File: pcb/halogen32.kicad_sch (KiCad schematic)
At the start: 13 parts, among them SW1 SW_SPDT, U1 STM32F411CEUx

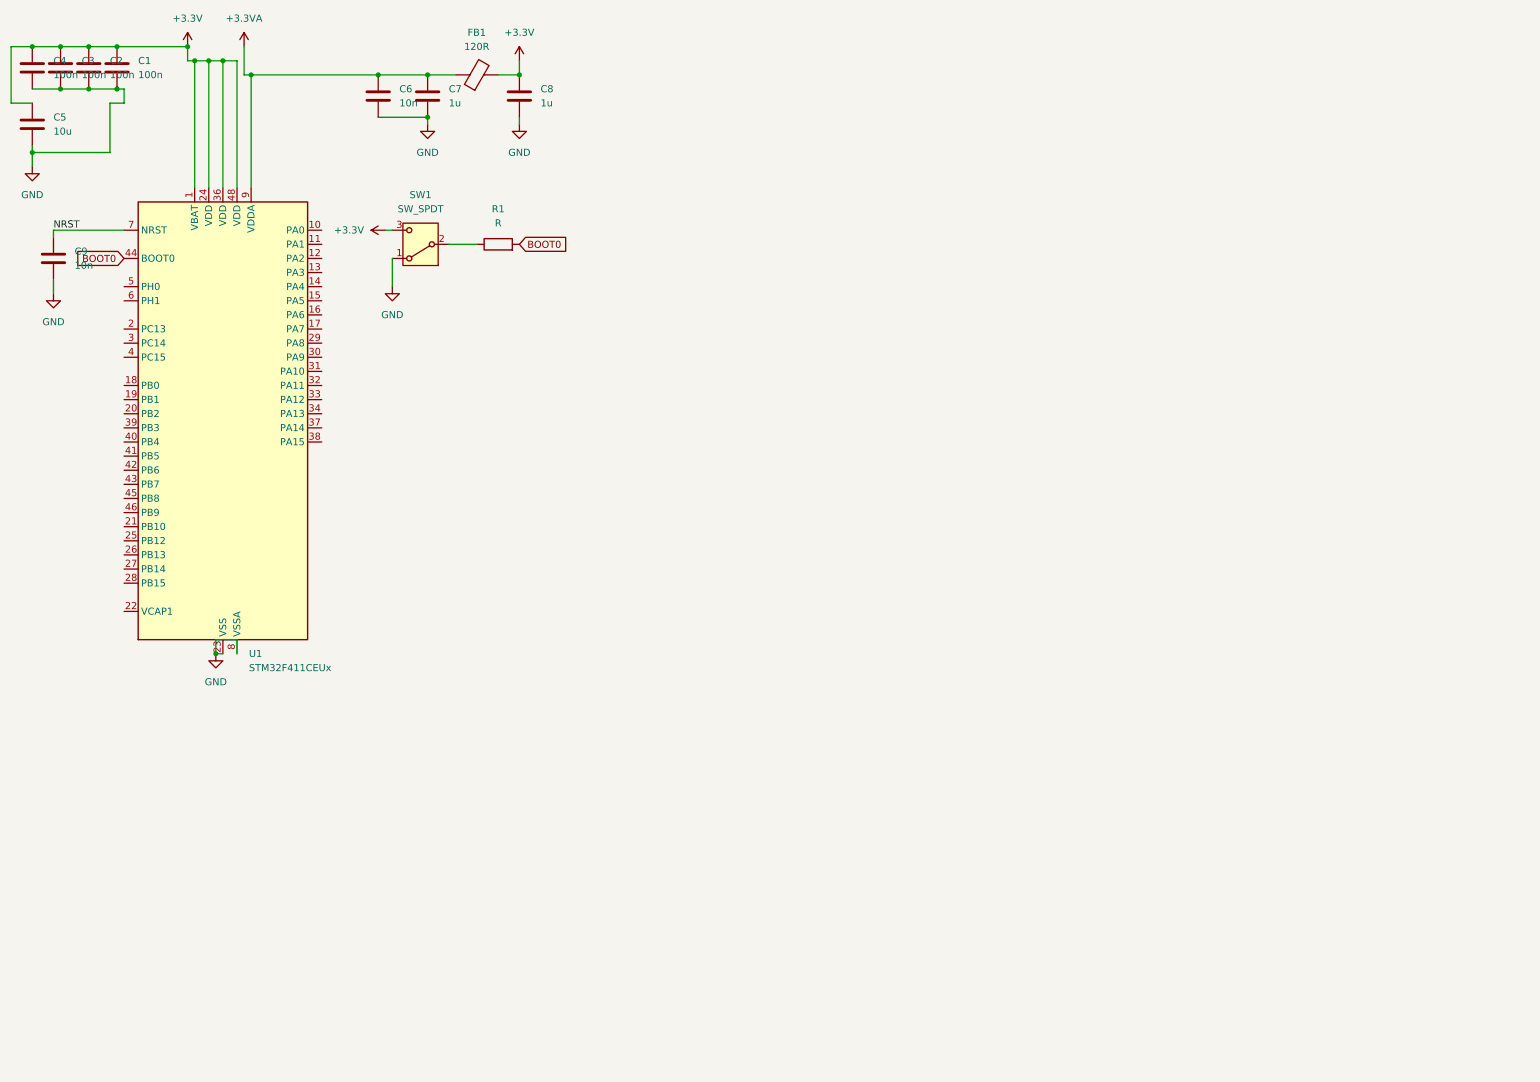
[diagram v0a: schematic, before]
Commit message: Reworked PCB design, added 2 neopixels, stemma-qt header, swd header, USB and stm32cubeide project files.
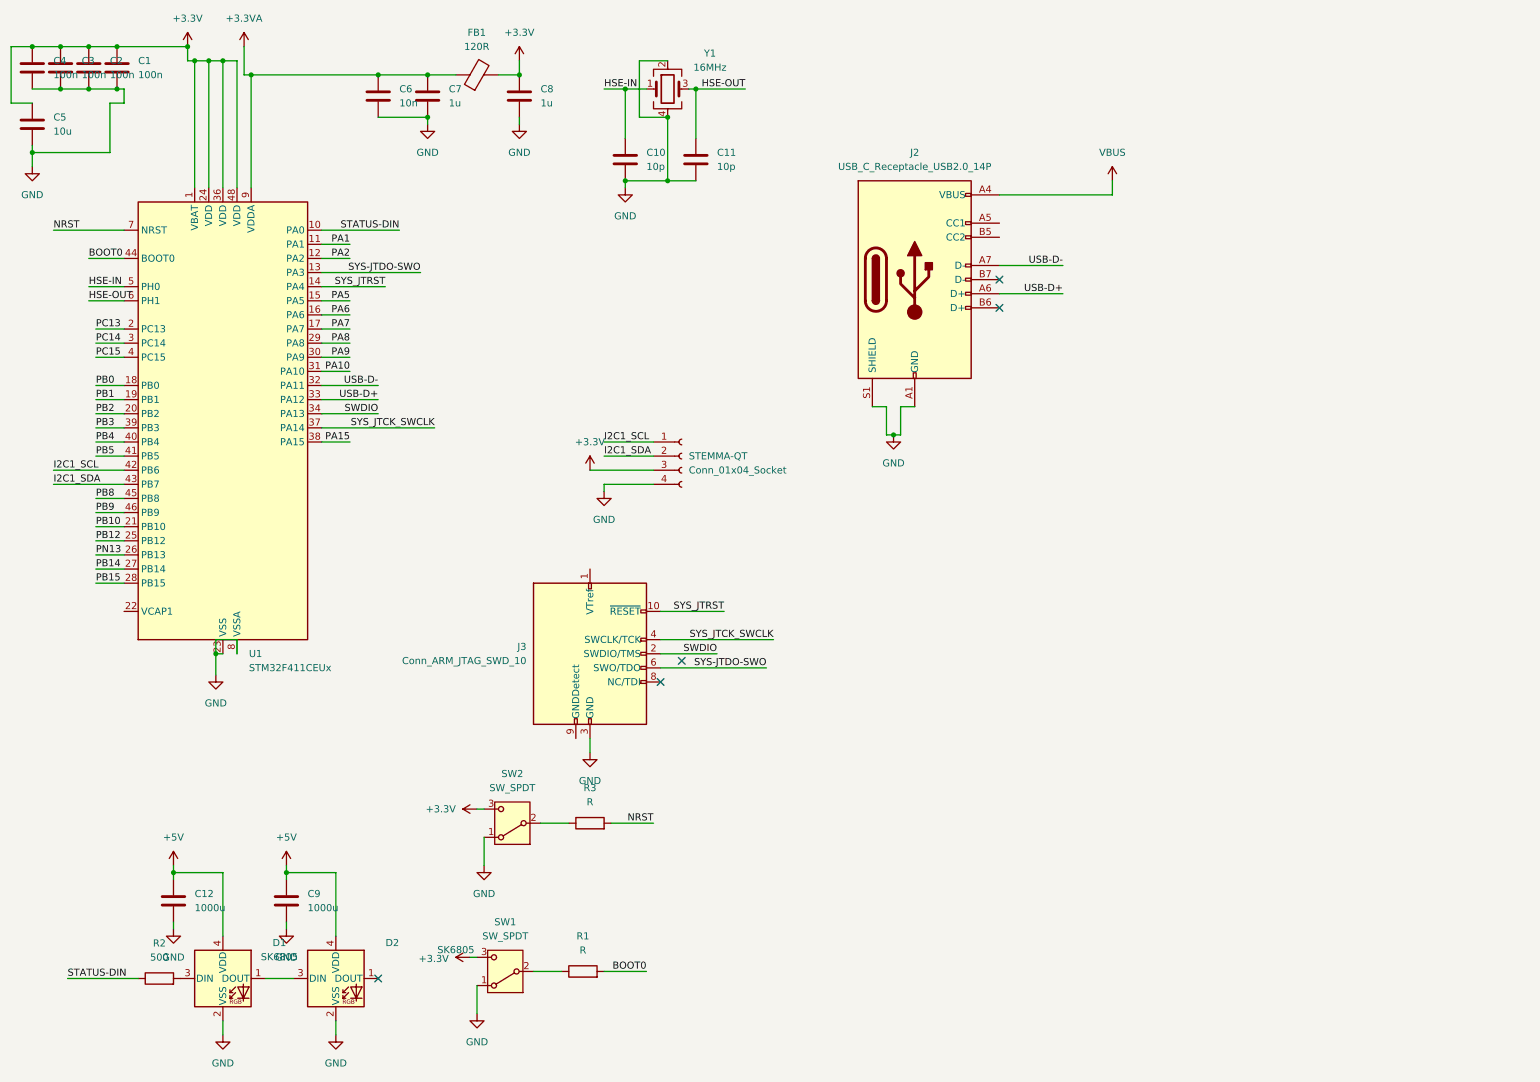
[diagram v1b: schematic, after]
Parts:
- added C10, C11: 10p, symbol Device:C
- added C12: 1000u, symbol Device:C
- added D1, D2: SK6805, LED_SMD:LED_SK6805_PLCC4_2.4x2.7mm_P1.3mm, symbol LED:SK6805
- added J2: USB_C_Receptacle_USB2.0_14P, symbol Connector:USB_C_Receptacle_USB2.0_14P
- added J3: Conn_ARM_JTAG_SWD_10, symbol Connector:Conn_ARM_JTAG_SWD_10
- added R2: 500, symbol Device:R
- added R3: R, symbol Device:R
- added STEMMA-QT: Conn_01x04_Socket, symbol Connector:Conn_01x04_Socket
- added SW2: SW_SPDT, symbol Switch:SW_SPDT
- added Y1: 16MHz, symbol Device:Crystal_GND24
- C9: value 10n -> 1000u
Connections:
- net +3.3V: now also STEMMA-QT.3 (Pin_3), SW2.3 (C)
- net GND: now also C10.2, C11.2, C12.2, D1.2 (VSS), D2.2 (VSS), J2.A1 (GND), J2.A12 (GND), J2.B1 (GND), J2.B12 (GND), J2.S1 (SHIELD), J3.3 (GND), J3.5 (GND), STEMMA-QT.4 (Pin_4), SW2.1 (A), Y1.2, Y1.4
- net NRST: now also R3.2; no longer C9.1
- net STATUS-DIN: now reaches U1.10 (PA0)
- net STATUS-DIN: now also R2.1
- net PA1: now reaches U1.11 (PA1)
- net PA2: now reaches U1.12 (PA2)
- net SYS-JTDO-SWO: now reaches U1.13 (PA3)
- net SYS-JTDO-SWO: now also J3.6 (SWO/TDO)
- net SYS_JTRST: now reaches U1.14 (PA4)
- net SYS_JTRST: now also J3.10 (~{RESET})
- net PA5: now reaches U1.15 (PA5)
- net PA6: now reaches U1.16 (PA6)
- net PA7: now reaches U1.17 (PA7)
- net PB0: now reaches U1.18 (PB0)
- net PB1: now reaches U1.19 (PB1)
- net PC13: now reaches U1.2 (PC13)
- net PB2: now reaches U1.20 (PB2)
- net PB10: now reaches U1.21 (PB10)
- net PB12: now reaches U1.25 (PB12)
- net PN13: now reaches U1.26 (PB13)
- net PB14: now reaches U1.27 (PB14)
- net PB15: now reaches U1.28 (PB15)
- net PA8: now reaches U1.29 (PA8)
- net PC14: now reaches U1.3 (PC14)
- net PA9: now reaches U1.30 (PA9)
- net PA10: now reaches U1.31 (PA10)
- net USB-D-: now reaches U1.32 (PA11)
- net USB-D-: now also J2.A7 (D-)
- net USB-D+: now reaches U1.33 (PA12)
- net USB-D+: now also J2.A6 (D+)
- net SWDIO: now reaches U1.34 (PA13)
- net SWDIO: now also J3.2 (SWDIO/TMS)
- net SYS_JTCK_SWCLK: now reaches U1.37 (PA14)
- net SYS_JTCK_SWCLK: now also J3.4 (SWCLK/TCK)
- net PA15: now reaches U1.38 (PA15)
- net PB3: now reaches U1.39 (PB3)
- net PC15: now reaches U1.4 (PC15)
- net PB4: now reaches U1.40 (PB4)
- net PB5: now reaches U1.41 (PB5)
- net I2C1_SCL: now reaches U1.42 (PB6)
- net I2C1_SCL: now also STEMMA-QT.1 (Pin_1)
- net I2C1_SDA: now reaches U1.43 (PB7)
- net I2C1_SDA: now also STEMMA-QT.2 (Pin_2)
- net PB8: now reaches U1.45 (PB8)
- net PB9: now reaches U1.46 (PB9)
- net HSE-IN: now reaches U1.5 (PH0)
- net HSE-IN: now also C10.1, Y1.1
- net HSE-OUT: now reaches U1.6 (PH1)
- net HSE-OUT: now also C11.1, Y1.3
- new net: D1.1 (DOUT), D2.3 (DIN)
- new net: R3.1, SW2.2 (B)
- new net: D1.3 (DIN), R2.2
- new net +5V: C12.1, C9.1, D1.4 (VDD), D2.4 (VDD)
- new net VBUS: J2.A4 (VBUS), J2.A9 (VBUS), J2.B4 (VBUS), J2.B9 (VBUS)
- no-connect marks 0 -> 5
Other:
- moved on the sheet: R1, SW1

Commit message: Added GPIO & 10pin SWD
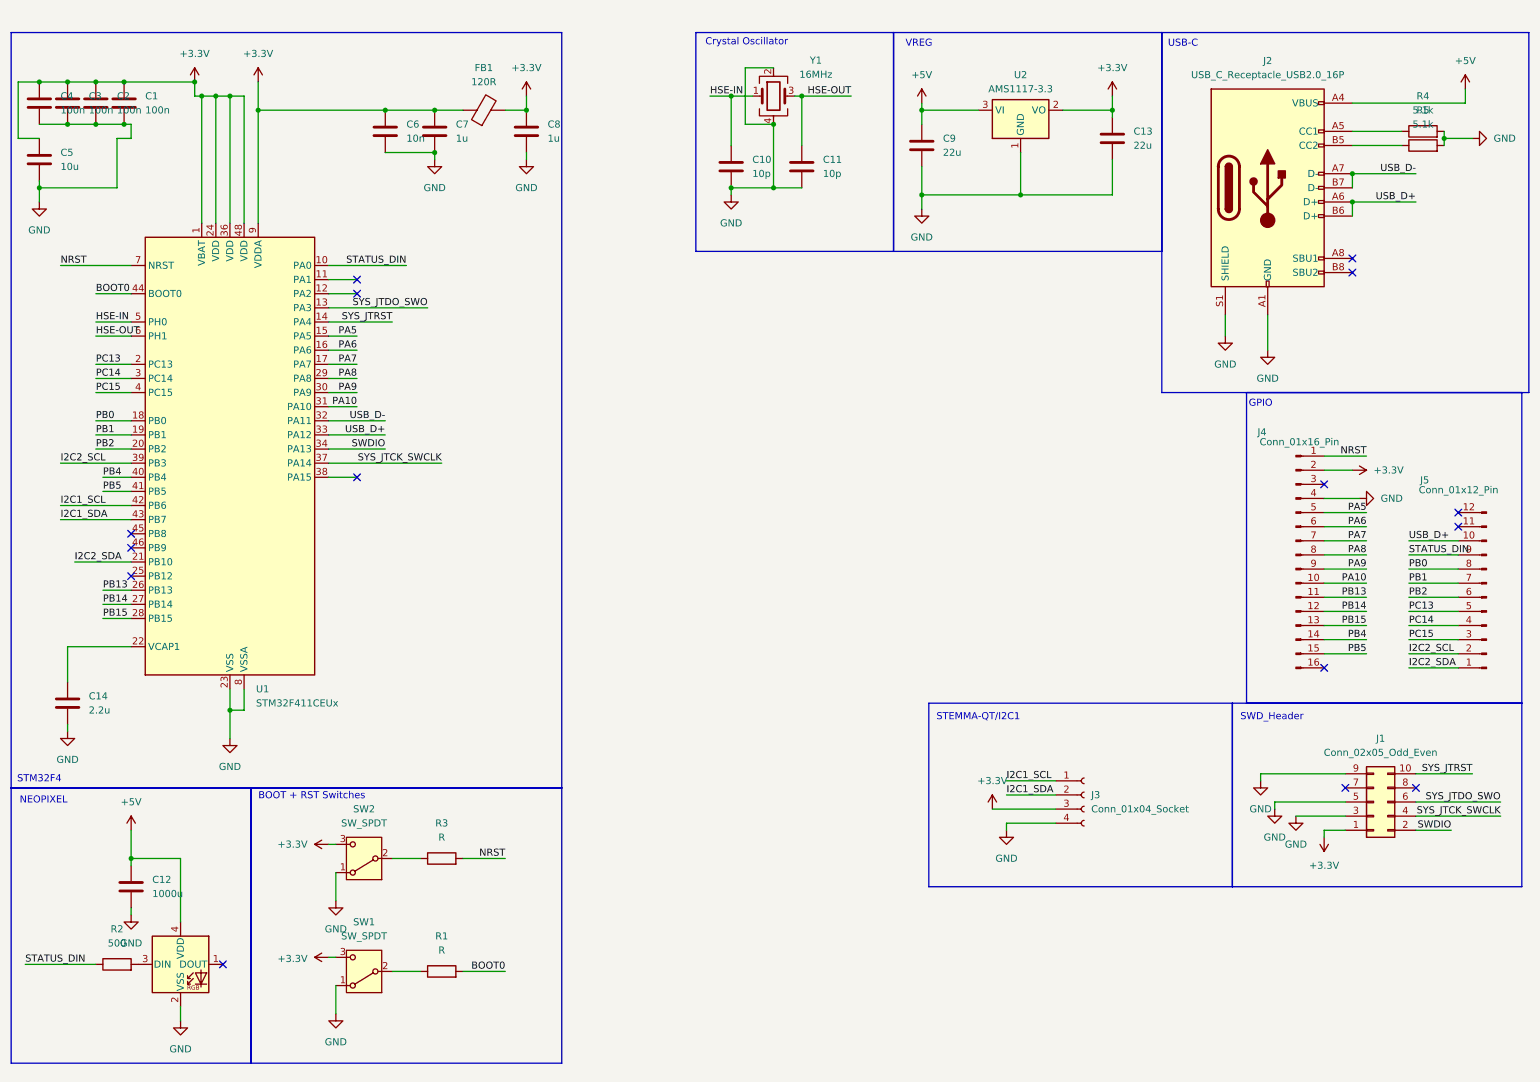
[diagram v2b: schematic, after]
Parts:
- removed D2: SK6805, LED_SMD:LED_SK6805_PLCC4_2.4x2.7mm_P1.3mm, symbol LED:SK6805
- removed J2: USB_C_Receptacle_USB2.0_14P, symbol Connector:USB_C_Receptacle_USB2.0_14P
- removed J3: Conn_ARM_JTAG_SWD_10, symbol Connector:Conn_ARM_JTAG_SWD_10
- added C13: 22u, symbol Device:C
- added C14: 2.2u, symbol Device:C
- added J1: Conn_02x05_Odd_Even, symbol Connector_Generic:Conn_02x05_Odd_Even
- added J2: USB_C_Receptacle_USB2.0_16P, symbol Connector:USB_C_Receptacle_USB2.0_16P
- added J4: Conn_01x16_Pin, symbol Connector:Conn_01x16_Pin
- added J5: Conn_01x12_Pin, symbol Connector:Conn_01x12_Pin
- added R4, R5: 5.1k, symbol Device:R
- added U2: AMS1117-3.3, Package_TO_SOT_SMD:SOT-223-3_TabPin2, symbol Regulator_Linear:AMS1117-3.3
- C9: value 1000u -> 22u
- renumbered STEMMA-QT to J3
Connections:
- net +3.3VA is gone; now on net +3.3V: C6.1, C7.1, FB1.1, U1.9 (VDDA)
- net +3.3V: now also C13.1, J1.1 (Pin_1), J4.2 (Pin_2), U2.2 (VO)
- net +5V: now also C9.2, J2.A4 (VBUS), J2.A9 (VBUS), J2.B4 (VBUS), J2.B9 (VBUS), U2.3 (VI); no longer C9.1
- net GND: now also C9.1, C13.2, C14.2, J1.3 (Pin_3), J1.5 (Pin_5), J1.9 (Pin_9), J2.A1 (GND), J2.A12 (GND), J2.B1 (GND), J2.B12 (GND), J2.S1 (SHIELD), J4.4 (Pin_4), R4.2, R5.2, U2.1 (GND); no longer C9.2
- net NRST: now also J4.1 (Pin_1)
- net PA10: now also J4.10 (Pin_10)
- net PA5: now also J4.5 (Pin_5)
- net PA6: now also J4.6 (Pin_6)
- net PA7: now also J4.7 (Pin_7)
- net PA8: now also J4.8 (Pin_8)
- net PA9: now also J4.9 (Pin_9)
- net PB0: now also J5.8 (Pin_8)
- net PB1: now also J5.7 (Pin_7)
- net PB14: now also J4.12 (Pin_12)
- net PB15: now also J4.13 (Pin_13)
- net PB2: now also J5.6 (Pin_6)
- net PB4: now also J4.14 (Pin_14)
- net PB5: now also J4.15 (Pin_15)
- net PC13: now also J5.5 (Pin_5)
- net PC14: now also J5.4 (Pin_4)
- net PC15: now also J5.3 (Pin_3)
- net SWDIO: now also J1.2 (Pin_2)
- net SYS_JTCK_SWCLK: now also J1.4 (Pin_4)
- net SYS_JTRST: now also J1.10 (Pin_10)
- net at U1.22 (VCAP1): now also C14.1
- net PA1: no longer names the net of U1.11 (PA1)
- net PA15: no longer names the net of U1.38 (PA15)
- net PA2: no longer names the net of U1.12 (PA2)
- net PB10 renamed I2C2_SDA
- net I2C2_SDA: now also J5.1 (Pin_1)
- net PB12: no longer names the net of U1.25 (PB12)
- net PB3 renamed I2C2_SCL
- net I2C2_SCL: now also J5.2 (Pin_2)
- net PB8: no longer names the net of U1.45 (PB8)
- net PB9: no longer names the net of U1.46 (PB9)
- net PN13 renamed PB13
- net PB13: now also J4.11 (Pin_11)
- net STATUS-DIN renamed STATUS_DIN
- net STATUS_DIN: now also J5.9 (Pin_9)
- net SYS-JTDO-SWO renamed SYS_JTDO_SWO
- net SYS_JTDO_SWO: now also J1.6 (Pin_6)
- net USB-D+ renamed USB_D+
- net USB_D+: now also J2.A6 (D+), J2.B6 (D+), J5.10 (Pin_10)
- net USB-D- renamed USB_D-
- net USB_D-: now also J2.A7 (D-), J2.B7 (D-)
- new net: J2.A5 (CC1), R4.1
- new net: J2.B5 (CC2), R5.1
- no-connect marks 5 -> 15
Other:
- note added: "BOOT + RST Switches"
- note added: "Crystal Oscillator"
- note added: "GPIO"
- note added: "NEOPIXEL"
- note added: "STEMMA-QT/I2C1"
- note added: "STM32F4"
- note added: "SWD_Header"
- note added: "USB-C"
- note added: "VREG"
- moved on the sheet: C1, C10, C11, C12, C2, C3, C4, C5, C6, C7, C8, FB1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
